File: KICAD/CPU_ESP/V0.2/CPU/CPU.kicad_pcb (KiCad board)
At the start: 2 copper layers, 95.2 x 95.2 mm, 89 parts, among them J101 USB_B_Micro, J102 Conn_01x04, J501 Conn_02x20_Odd_Even, J502 Conn_02x20_Odd_Even, Q401 BC817, Q402 BC807, Q601 BSR19, Q602 BSR19, SW101 SW_Push_45deg, SW102 SW_Push_45deg, U201 LM75A, U202 PCA9306, U203 PCF8563T, U204 TCA9544A, U205 MCP23017_SS, U207 AT24CS01-SSHM, U301 LM1117DT-2.5, U401 ESP32-WROOM-32, U402 FT4232H, U403 TJA1051T, U404 93C46, U405 74HC02, U406 74HC244, U601 SAA1064T, Y201 32.278kHz

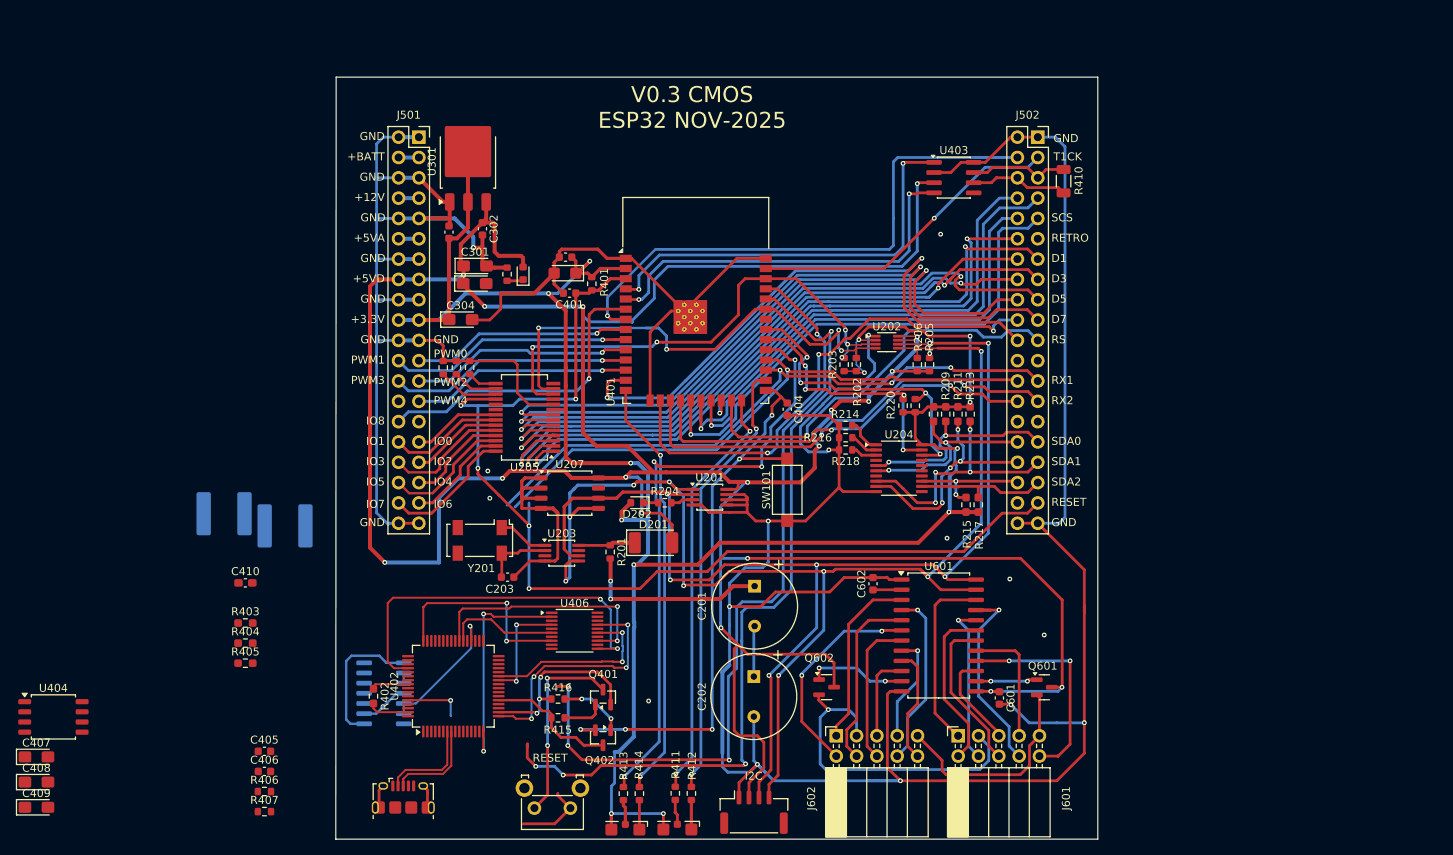
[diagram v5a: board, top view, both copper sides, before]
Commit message: KICAD 4 UART update
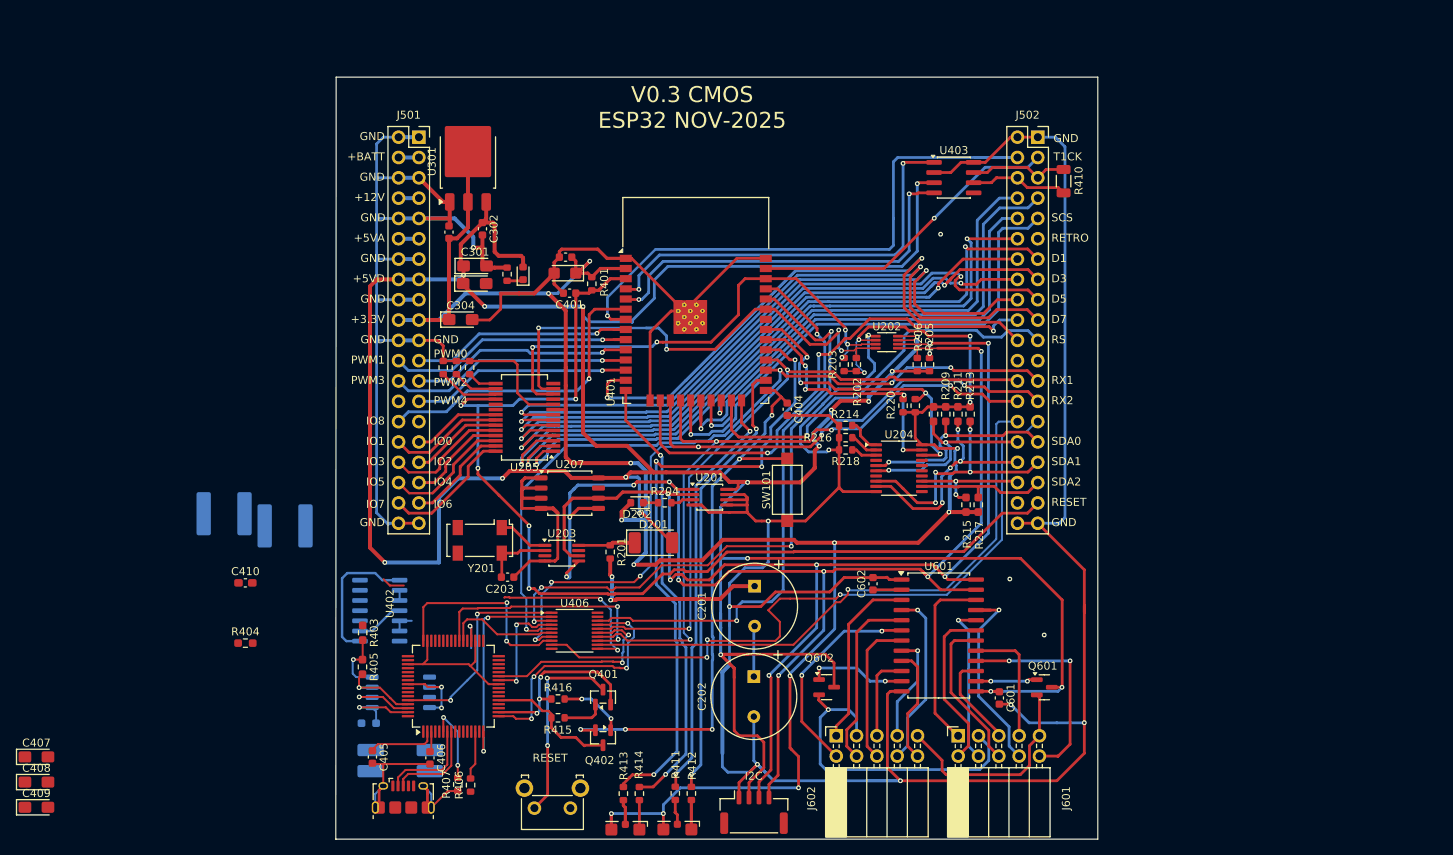
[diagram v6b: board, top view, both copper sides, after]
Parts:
- added Y401: 12Mhz, Crystal:Crystal_SMD_EuroQuartz_MQ-4Pin_7.0x5.0mm_HandSoldering, B.Cu at (95.6, 147.5)
- R402, U404: moved to B.Cu
- U402: footprint Package_QFP:TQFP-64_10x10mm_P0.5mm -> Package_QFP:LQFP-64_10x10mm_P0.5mm
- moved U404 43.5 mm to (95.7, 139.0)
- moved R406 25.8 mm to (104.4, 150.6), turned to 90 degrees
- moved R407 24.4 mm to (102.8, 150.5), turned to 90 degrees
- moved C406 20.8 mm to (99.4, 147.2), turned to -90 degrees
- moved R403 14.7 mm to (91.0, 131.6), turned to -90 degrees
- moved R405 14.6 mm to (90.9, 135.8), turned to -90 degrees
- moved C405 13.5 mm to (92.2, 147.1), turned to -90 degrees
- moved U405 10.3 mm to (93.1, 128.8)
- moved R402 3.43 mm to (91.7, 142.9), turned to 0 degrees
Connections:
- net /RX0 renamed /ESP32 Module/RX0
- net /TX0 renamed /ESP32 Module/TX0
- J502 pad 29: /CMOS_BUS/UART-RX3 -> /RX3
- J502 pad 30: /CMOS_BUS/UART-TX3 -> /TX3
- U406 pad 12: /ESP32 Module/TX3 -> /TX3
- U406 pad 9: /ESP32 Module/RX3 -> /RX3
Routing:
- net /RX3: track 0.00 -> 86.5 mm, vias 0 -> 3
- net /TX3: track 0.00 -> 72.9 mm, vias 0 -> 1
- net /RX2: track 56.3 -> 99.9 mm, vias 2 -> 6
- net /TX2: track 51.1 -> 90.0 mm, vias 2 -> 4
- net GND: track 569.9 -> 600.0 mm, vias 17 -> 14
- net /ESP32 Module/TX0: track 99.8 -> 69.9 mm, vias 4 -> 2
- net +3.3V: track 275.7 -> 300.4 mm, vias 13 -> 18
- net /ESP32 Module/RX0: track 102.7 -> 80.3 mm
- net /ESP32 Module/RX3A: track 47.2 -> 24.9 mm
- net Net-(U402-~{PWREN}): track 8.56 -> 28.2 mm, vias 1 -> 2
- net /RX1: track 78.1 -> 96.5 mm, vias 3 -> 4
- net Net-(U402-EEDATA): track 0.00 -> 10.5 mm, vias 0 -> 1
- net Net-(U402-REF): track 0.00 -> 10.1 mm, vias 0 -> 2
- net Net-(U402-~{SUSPEND}): track 17.3 -> 7.53 mm
- net Net-(U402-OSCI): track 0.00 -> 8.65 mm
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
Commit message: KICAD 4 UART Update
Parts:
- C408, C409, R404: moved to B.Cu
- moved C408 59.3 mm to (106.8, 132.8)
- moved C407 58.8 mm to (109.0, 147.8)
- moved C409 54.7 mm to (104.8, 150.7)
- moved C410 39.1 mm to (106.0, 150.8), turned to 90 degrees
- moved L401 38.9 mm to (106.9, 136.9)
- moved L402 36.0 mm to (107.0, 143.5)
- moved R404 18.7 mm to (94.8, 134.9), turned to 180 degrees
- moved R402 1.83 mm to (93.6, 143.0), turned to 180 degrees
- moved Y401 1.37 mm to (94.4, 146.9)
- moved J101 0.69 mm to (96.1, 152.8)
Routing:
- net GND: track 600.0 -> 738.3 mm, vias 14 -> 16
- net +3.3V: track 300.4 -> 424.2 mm, vias 18 -> 26
- net Net-(U406-2OE): track 0.00 -> 36.6 mm, vias 0 -> 3
- net Net-(U402-VREGOUT): track 0.00 -> 33.5 mm, vias 0 -> 2
- net /ESP32 Module/RX3A: track 24.9 -> 49.2 mm
- net Net-(U402-VPHY): track 0.00 -> 18.0 mm, vias 0 -> 1
- net Net-(U402-VPLL): track 0.00 -> 17.0 mm, vias 0 -> 1
- net Net-(U402-~{PWREN}): track 28.2 -> 44.4 mm, vias 2 -> 4
- net /RESET: track 158.7 -> 171.0 mm
- net Net-(U402-~{SUSPEND}): track 7.53 -> 16.8 mm, vias 1 -> 3
- net Net-(U402-EECLK): track 8.30 -> 14.5 mm
- net /D6: track 81.3 -> 76.9 mm
- net /D7: track 84.9 -> 81.4 mm
- net /RW: track 93.5 -> 91.0 mm
- net Net-(U402-EECS): track 10.1 -> 12.3 mm
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- added copper zone on B.Cu, net GND
- added copper zone on F.Cu, net GND

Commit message: KICAD 4 UART Update V 0.3
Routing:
- net +5VD: track 429.3 -> 413.1 mm
- net /D6: track 76.9 -> 91.4 mm
- net +3.3V: track 424.2 -> 420.7 mm
- net /D3: track 84.9 -> 82.0 mm
- net Net-(U401-IO5): track 79.4 -> 77.0 mm
- net Net-(U401-IO12): track 55.9 -> 53.8 mm
- net /SDA: track 63.4 -> 65.4 mm
- net /SCL-5V: track 153.3 -> 154.8 mm
- net /TX2: track 90.0 -> 88.9 mm
- net /SCL: track 63.9 -> 64.9 mm
- net Net-(U402-~{SUSPEND}): track 16.8 -> 16.1 mm
- net /RESET: track 171.0 -> 170.4 mm
- net GND: track 738.3 -> 737.7 mm, vias 16 -> 18
- net /SDA-5V: track 159.6 -> 160.1 mm
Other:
- board text added: "CANH"
- board text added: "CANL"
- board text added: "D0"
- board text added: "D2"
- board text added: "D4"
- board text added: "D6"
- board text added: "E"
- board text added: "INT0"
- board text added: "INT1"
- board text added: "IO9"
- board text added: "RW"
- board text added: "RX0"
- board text added: "RX3"
- board text added: "SCK"
- board text added: "SCL0"
- board text added: "SCL1"
- board text added: "SCL2"
- board text added: "SDI"
- board text added: "SDO"
- board text added: "T2CK"
- board text added: "TX0"
- board text added: "TX1"
- board text added: "TX2"
- board text added: "TX3"
